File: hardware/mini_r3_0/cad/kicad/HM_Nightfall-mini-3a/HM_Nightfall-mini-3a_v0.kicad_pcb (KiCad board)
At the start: 2 copper layers, 39 x 70 mm, 97 parts, among them J2 FAN_2S3S, K1 62201021121, P1 BATTERY, Q2 SI7135DP-T1-GE3, Q3 IRLML6344TRPBF, U1 AP2210N-3.3TRG1, U2 MP6551GQB-P, U3 MP6551GQB-P, U4 ISM330DHCXTR, U5 STM32F413CHU6TRUFQFPN-48_7X7X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, U6 CY15B108QI-20LPXC, U7 MPM3610GQV-P

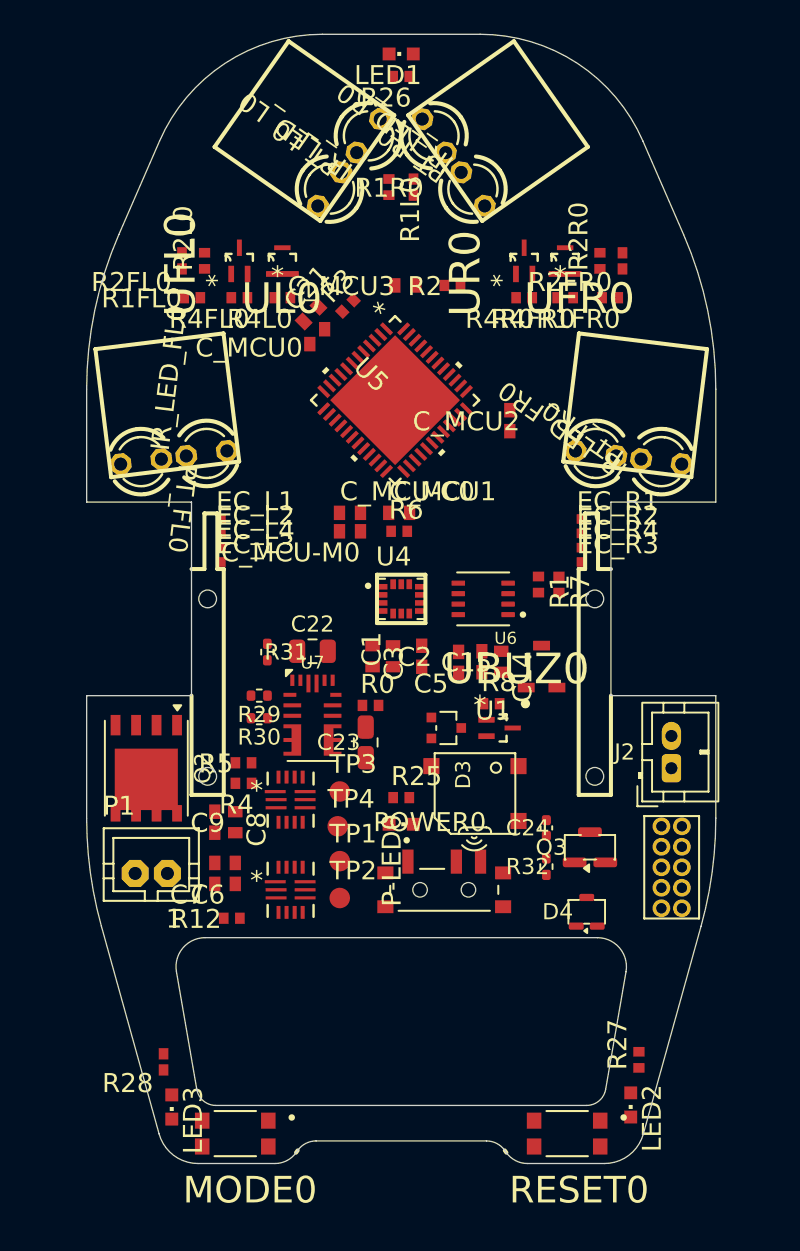
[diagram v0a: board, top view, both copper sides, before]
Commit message: Replace mini_r3 PCB with final DXF
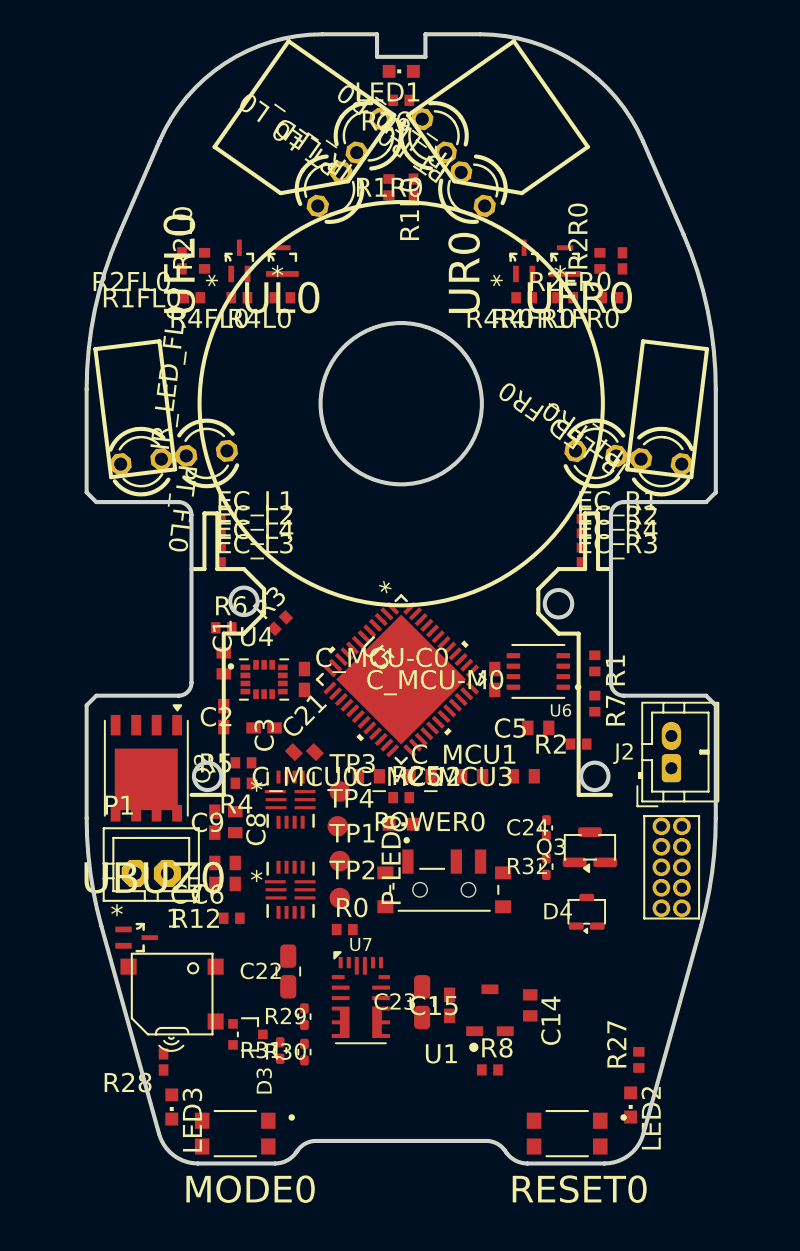
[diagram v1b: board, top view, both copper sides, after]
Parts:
- moved C_MCU3 31.3 mm to (156.1, 116.0)
- moved R2 29.5 mm to (159.5, 114.0)
- moved C_MCU0 27.4 mm to (146.5, 116.0), turned to 0 degrees
- moved C21 27.2 mm to (142.5, 114.5), turned to 0 degrees
- moved UBUZ0 26.0 mm to (132.1, 126.0)
- moved R31 24.7 mm to (141.0, 133.0), turned to 90 degrees
- moved R8 22.7 mm to (154.0, 134.2)
- moved D3 22.6 mm to (139.0, 132.0)
- moved SPK1 22.5 mm to (134.3, 129.5)
- moved C_MCU2 22.2 mm to (152.9, 116.0), turned to 0 degrees
- moved U1 21.5 mm to (154.0, 130.5)
- moved C15 21.4 mm to (151.5, 130.2)
- moved C14 21.4 mm to (156.5, 130.2)
- moved R30 20.9 mm to (142.5, 133.1), turned to 90 degrees
- moved R3 20.1 mm to (141.0, 106.5)
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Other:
- outline, holes or cut-outs redrawn

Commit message: Refine mini_r3 fan and control placement
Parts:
- J2: footprint Connector_JST:JST_PH_B2B-PH-K_1x02_P2.00mm_Vertical -> HM_Nightfall-mini-2e_v1:FAN_WIRE_PADS_2P
- Q2: value SI7135DP-T1-GE3 -> IRLML6402TRPBF; footprint Nightfall-Power:PowerPAK_SO-8_FullPins -> Package_TO_SOT_SMD:SOT-23
- moved J2 35.0 mm to (132.0, 104.5), turned to 0 degrees
- moved POWER0 13.2 mm to (148.5, 136.0)
- moved UL0 10.8 mm to (131.8, 89.5)
- moved UR0 10.6 mm to (165.2, 89.5)
- moved R4L0 7.86 mm to (134.6, 90.7)
- moved R4R0 7.65 mm to (162.4, 90.7)
- moved R1FL0 7.14 mm to (133.0, 93.0)
- moved R1FR0 7.13 mm to (164.0, 93.0)
- moved UFL0 6.68 mm to (131.8, 84.5)
- moved UFR0 6.55 mm to (165.2, 84.5)
- moved PT_FL0 6.07 mm to (132.4, 100.5), turned to 7 degrees
- moved PT_FR0 6.07 mm to (164.6, 100.5), turned to 173 degrees
- moved R2L0 4.77 mm to (134.6, 88.5)
- moved R2R0 4.72 mm to (162.4, 88.5)
- moved R4FL0 3.92 mm to (134.6, 85.7)
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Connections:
- Q2 pad 1: VBAT_RAW -> /PWR_GATE_INTERNAL
- Q2 pad 3: VBAT_RAW -> VBAT_SW

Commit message: Refine mini_r3 sensor and IMU placement
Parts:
- moved U4 8.73 mm to (148.5, 108.0)
- moved C_MCU0 6.39 mm to (144.3, 110.0), turned to -90 degrees
- moved C_MCU1 6.30 mm to (156.0, 116.2), turned to -90 degrees
- moved C_MCU2 6.00 mm to (152.7, 110.0), turned to -90 degrees
- moved U5 4.20 mm to (148.5, 114.7)
- moved TP3 3.86 mm to (144.7, 120.8)
- moved P-LED0 3.83 mm to (148.5, 122.8)
- moved R25 3.68 mm to (148.5, 121.0)
- moved PT_FL0 2.99 mm to (132.4, 97.5)
- moved PT_FR0 2.99 mm to (164.6, 97.5)
- moved C_MCU3 2.16 mm to (154.0, 116.5), turned to -90 degrees
- moved TP1 1.04 mm to (144.7, 122.3)
- moved POWER0 0.90 mm to (148.5, 136.9)
- moved IR_LED_FL0 0.79 mm to (132.4, 95.7)
- moved IR_LED_FR0 0.79 mm to (164.6, 95.7)
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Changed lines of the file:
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@@
 	(footprint "HM_Nightfall-mini-2e_v1:LED3MM"
 		(layer "F.Cu")
-		(at 164.630098 100.494598 173)
+		(at 164.630098 97.5 173)
 		(descr "LED\n\n3 mm, round")
 		(property "Reference" "PT_FR0"
@@
 	(footprint "HM_Nightfall-mini-2e_v1:B1,27"
 		(layer "F.Cu")
-		(at 144.691098 123.545598)
+		(at 144.691098 123.8)
 		(descr "TEST PAD")
 		(property "Reference" "TP2"
@@
 	(footprint "HM_Nightfall-mini-2e_v1:B1,27"
 		(layer "F.Cu")
-		(at 144.691098 121.259598)
+		(at 144.691098 122.3)
 		(descr "TEST PAD")
 		(property "Reference" "TP1"
@@
 	(footprint "HM_Nightfall-mini-2e_v1:B1,27"
 		(layer "F.Cu")
-		(at 144.691098 116.941598)
+		(at 144.691098 120.8)
 		(descr "TEST PAD")
 		(property "Reference" "TP3"
@@
 	(footprint "HM_Nightfall-mini-2e_v1:R0402"
 		(layer "F.Cu")
-		(at 148.501098 117.322598)
+		(at 148.501098 121)
 		(descr "Chip RESISTOR 0402 EIA (1005 Metric)")
 		(property "Reference" "R25"
@@
 	(footprint "HM_Nightfall-mini-2e_v1:CHIPLED_0603"
 		(layer "F.Cu")
-		(at 148.501098 118.973598 -90)
+		(at 148.501098 122.8 -90)
 		(descr "CHIPLED\n\nSource: http://www.osram.convergy.de/ ... LG_LY Q971.pdf")
 		(property "Reference" "P-LED0"
@@
 	(footprint "HM_Nightfall-mini-2e_v1:C0402"
 		(layer "F.Cu")
-		(at 146.5 116)
+		(at 144.3 110 -90)
 		(descr "CAPACITOR")
 		(property "Reference" "C_MCU0"
@@
 	(footprint "HM_Nightfall-mini-2e_v1:LED3MM"
 		(layer "F.Cu")
-		(at 132.372098 100.494598 7)
+		(at 132.372098 97.5 7)
 		(descr "LED\n\n3 mm, round")
 		(property "Reference" "PT_FL0"
@@
 	(footprint "HM_Nightfall-mini-2e_v1:UFQFPN-48_7X7X0P55MM-M"
 		(layer "F.Cu")
-		(at 148.5 110.5 -45)
+		(at 148.501098 114.7 -45)
 		(property "Reference" "U5"
 			(at -3.276597 0.635002 315)
@@
 	(footprint "HM_Nightfall-mini-2e_v1:C0402"
 		(layer "F.Cu")
-		(at 156.1 116)
+		(at 154 116.5 -90)
 		(descr "CAPACITOR")
 		(property "Reference" "C_MCU3"
@@
 	(footprint "HM_Nightfall-mini-2e_v1:LED3MM"
 		(layer "F.Cu")
-		(at 132.372098 96.494598 7)
+		(at 132.372098 95.7 7)
 		(descr "LED\n\n3 mm, round")
 		(property "Reference" "IR_LED_FL0"
@@
 	(footprint "HM_Nightfall-mini-2e_v1:C0402"
 		(layer "F.Cu")
-		(at 152.9 116)
+		(at 152.7 110 -90)
 		(descr "CAPACITOR")
 		(property "Reference" "C_MCU2"
@@
 	(footprint "HM_Nightfall-mini-2e_v1:LED3MM"
 		(layer "F.Cu")
-		(at 164.630098 96.494598 173)
+		(at 164.630098 95.7 173)
 		(descr "LED\n\n3 mm, round")
 		(property "Reference" "IR_LED_FR0"
@@
 	(footprint "HM_Nightfall-mini-2e_v1:SW_EG1215AA"
 		(layer "F.Cu")
-		(at 148.501098 136)
+		(at 148.501098 136.903598)
 		(property "Reference" "POWER0"
 			(at -4.4 -3.496 0)
@@
 	(footprint "HM_Nightfall-mini-2e_v1:PQFN50P250X300X86-14N"
 		(layer "F.Cu")
-		(at 140 110)
+		(at 148.501098 108)
 		(property "Reference" "U4"
 			(at -1.5748 -1.9304 0)
@@
 	(footprint "HM_Nightfall-mini-2e_v1:C0402"
 		(layer "F.Cu")
-		(at 149.7 116)
+		(at 156 116.2 -90)
 		(descr "CAPACITOR")
 		(property "Reference" "C_MCU1"

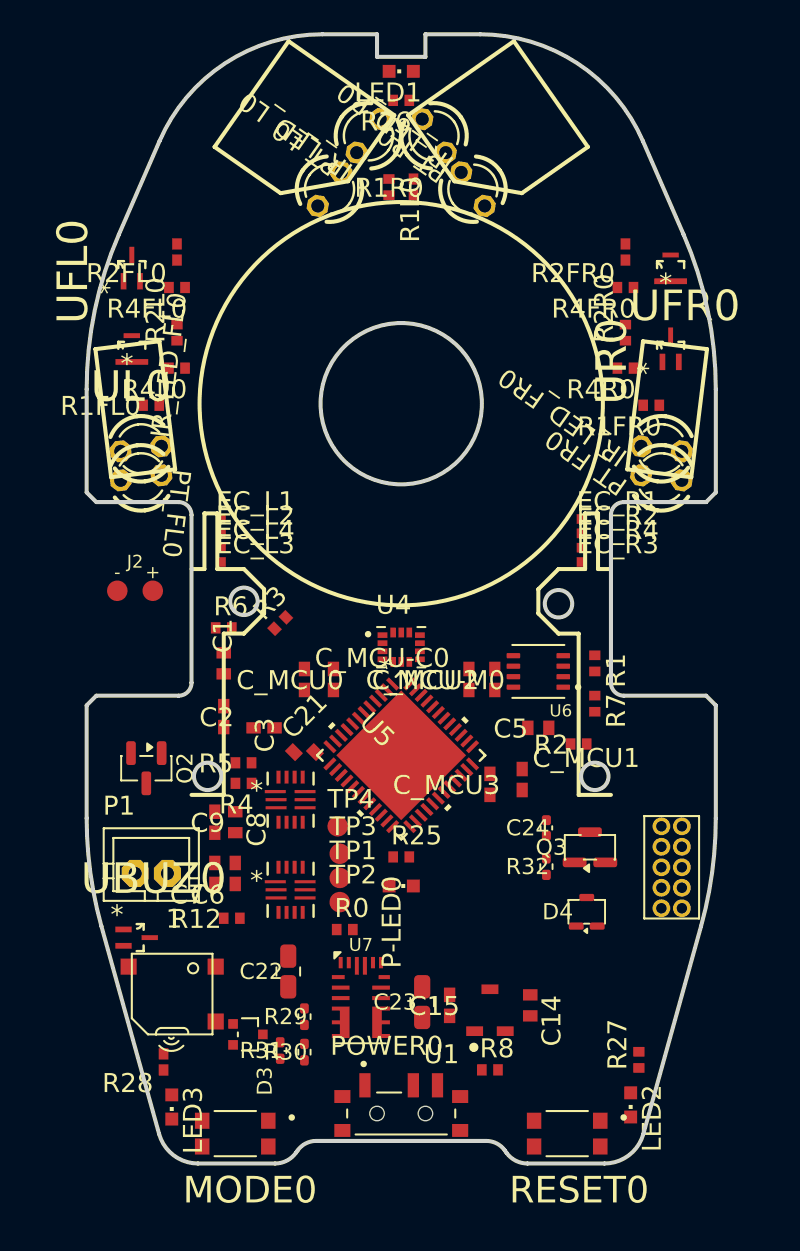
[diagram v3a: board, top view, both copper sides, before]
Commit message: Refine mini_r3 fan and sensor keepouts
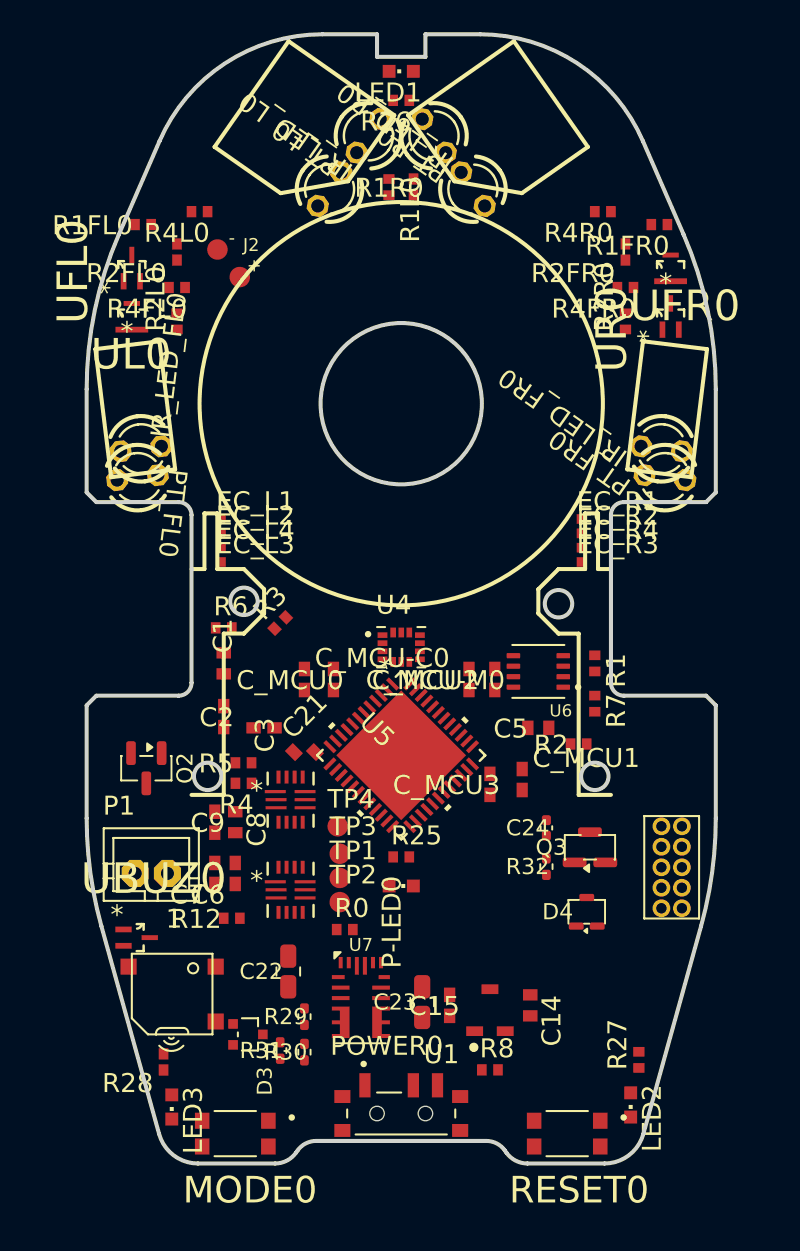
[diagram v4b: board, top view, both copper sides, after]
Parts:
- moved J2 21.1 mm to (137.8, 84.2), turned to -51 degrees
- moved R1FL0 11.2 mm to (132.5, 81.8)
- moved R1FR0 11.2 mm to (164.5, 81.8)
- moved R4L0 9.80 mm to (136.0, 81.0)
- moved R4R0 9.80 mm to (161.0, 81.0)
- moved UL0 2.00 mm to (131.8, 87.5)
- moved UR0 2.00 mm to (165.2, 87.5)
- moved R2L0 0.70 mm to (134.6, 87.8)
- moved R2R0 0.70 mm to (162.4, 87.8)
- moved PT_FL0 0.22 mm to (132.2, 97.5)
- moved PT_FR0 0.22 mm to (164.8, 97.5)
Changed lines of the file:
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@@
 	(footprint "HM_Nightfall-mini-2e_v1:SOT50P160X90-3N"
 		(layer "F.Cu")
-		(at 131.8 89.5 90)
+		(at 131.8 87.5 90)
 		(property "Reference" "UL0"
 			(at -3.456619 -2.541632 0)
@@
 	(footprint "HM_Nightfall-mini-2e_v1:R0402"
 		(layer "F.Cu")
-		(at 164 93 180)
+		(at 164.5 81.8 180)
 		(descr "Chip RESISTOR 0402 EIA (1005 Metric)")
 		(property "Reference" "R1FR0"
@@
 	(footprint "HM_Nightfall-mini-2e_v1:LED3MM"
 		(layer "F.Cu")
-		(at 164.630098 97.5 173)
+		(at 164.849463 97.486583 173)
 		(descr "LED\n\n3 mm, round")
 		(property "Reference" "PT_FR0"
@@
 	(footprint "HM_Nightfall-mini-2e_v1:R0402"
 		(layer "F.Cu")
-		(at 162.4 88.5 90)
+		(at 162.4 87.8 90)
 		(descr "Chip RESISTOR 0402 EIA (1005 Metric)")
 		(property "Reference" "R2R0"
@@
 	(footprint "HM_Nightfall-mini-2e_v1:R0402"
 		(layer "F.Cu")
-		(at 134.6 88.5 90)
+		(at 134.6 87.8 90)
 		(descr "Chip RESISTOR 0402 EIA (1005 Metric)")
 		(property "Reference" "R2L0"
@@
 	(footprint "HM_Nightfall-mini-2e_v1:SOT50P160X90-3N"
 		(layer "F.Cu")
-		(at 165.2 89.5 90)
+		(at 165.2 87.5 90)
 		(property "Reference" "UR0"
 			(at -3.456619 -2.541632 90)
@@
 	(footprint "HM_Nightfall-mini-2e_v1:R0402"
 		(layer "F.Cu")
-		(at 162.4 90.7 180)
+		(at 161 81 180)
 		(descr "Chip RESISTOR 0402 EIA (1005 Metric)")
 		(property "Reference" "R4R0"
@@
 	(footprint "HM_Nightfall-mini-2e_v1:LED3MM"
 		(layer "F.Cu")
-		(at 132.372098 97.5 7)
+		(at 132.152733 97.486583 7)
 		(descr "LED\n\n3 mm, round")
 		(property "Reference" "PT_FL0"
@@
 	(footprint "HM_Nightfall-mini-2e_v1:R0402"
 		(layer "F.Cu")
-		(at 134.6 90.7 180)
+		(at 136 81 180)
 		(descr "Chip RESISTOR 0402 EIA (1005 Metric)")
 		(property "Reference" "R4L0"
@@
 	(footprint "HM_Nightfall-mini-2e_v1:R0402"
 		(layer "F.Cu")
-		(at 133 93)
+		(at 132.5 81.8)
 		(descr "Chip RESISTOR 0402 EIA (1005 Metric)")
 		(property "Reference" "R1FL0"
@@
 	(footprint "HM_Nightfall-mini-2e_v1:FAN_WIRE_PADS_2P"
 		(layer "F.Cu")
-		(at 132 104.5)
+		(at 137.8 84.2 -51)
 		(descr "Two direct-solder wire pads using the mini-2e motor-pad geometry")
 		(tags "fan wire solder pad mini-2e")

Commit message: Clear mini_r3 motor mount keepouts
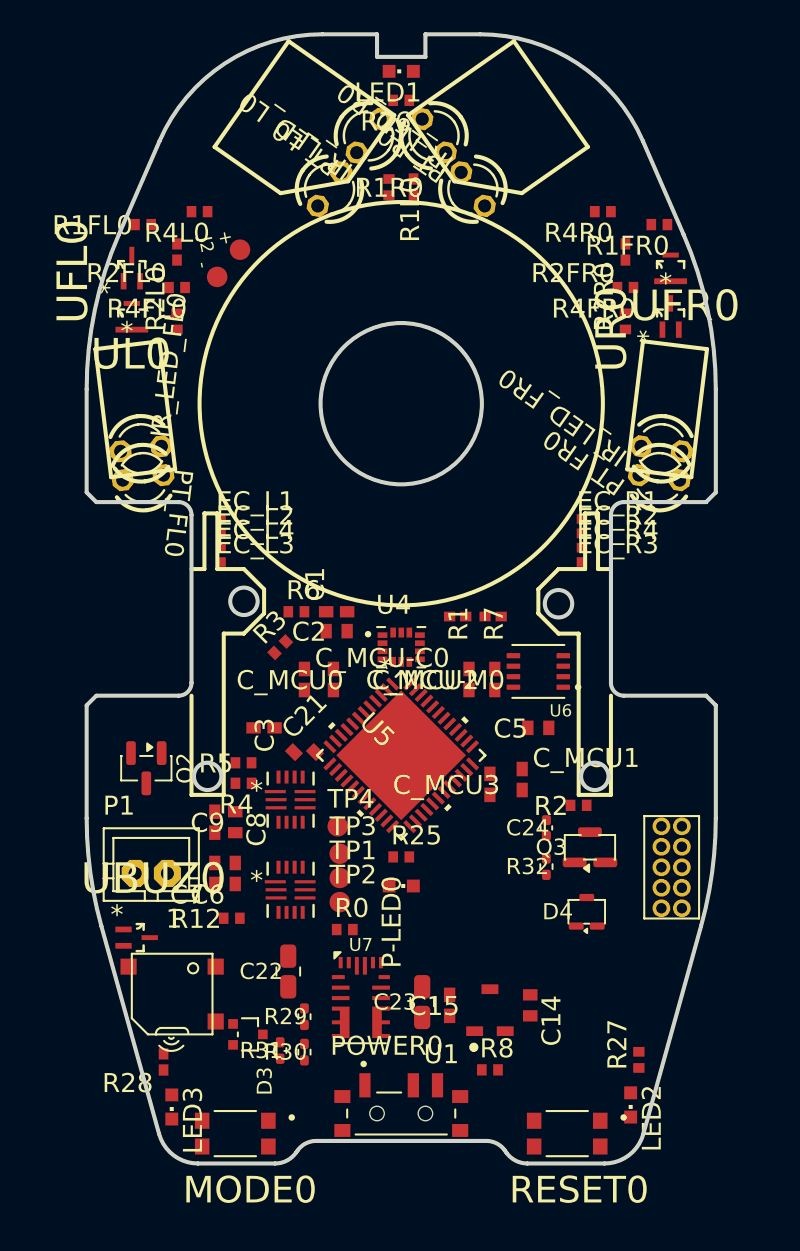
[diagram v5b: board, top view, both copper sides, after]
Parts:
- moved R1 8.98 mm to (152.0, 106.1), turned to 0 degrees
- moved C2 8.78 mm to (144.5, 107.0), turned to 0 degrees
- moved R7 8.30 mm to (154.2, 106.1), turned to 0 degrees
- moved C1 7.70 mm to (144.5, 105.8), turned to 0 degrees
- moved R6 4.61 mm to (142.0, 105.8)
- moved R2 3.80 mm to (159.5, 117.8)
- moved R3 1.50 mm to (141.0, 108.0)
- moved PT_FR0 0.35 mm to (164.5, 97.5)
- moved PT_FL0 0.35 mm to (132.5, 97.5)
- turned J2 to 50 degrees
